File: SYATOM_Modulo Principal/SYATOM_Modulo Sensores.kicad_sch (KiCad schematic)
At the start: 27 parts, among them J1 Input, J10 Head_HX711_2, J11 Head_HX711, J12 Exp_GPIO, J13 Exp_ADC, J14 Exp_I2C, J15 PWM_A, J16 PWM_B, J17 Header_Max485_1, J18 Header_Max3232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

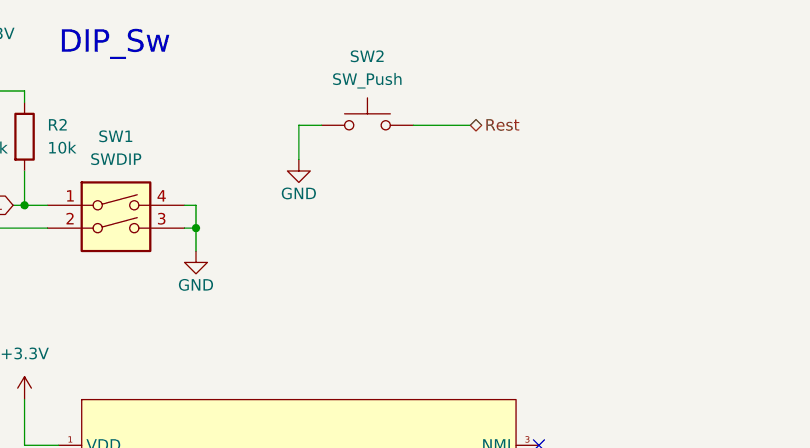
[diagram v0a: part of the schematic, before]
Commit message: Add files via upload
Se agrego el silkscreen de los logos y label de los conectores, ademas una resistencia pull-up al botón reset
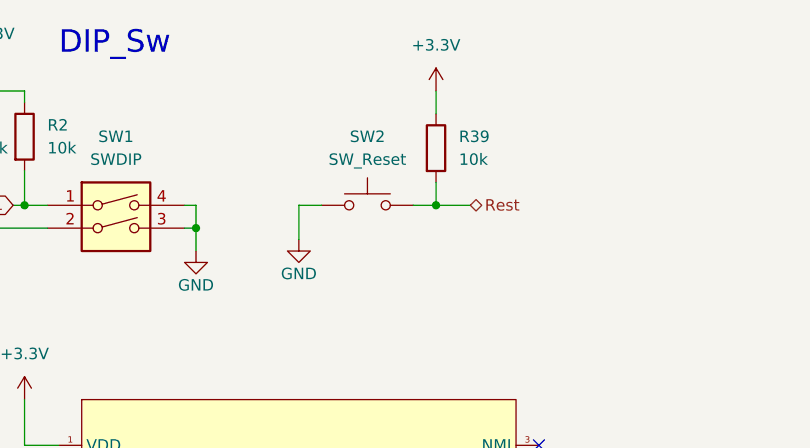
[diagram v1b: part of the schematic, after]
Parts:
- added R39: 10k, Resistor_SMD:R_0603_1608Metric, symbol Device:R
- SW2: value SW_Push -> SW_Reset
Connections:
- net +3V3: now also R39.1
- net Rest: now also R39.2
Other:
- moved on the sheet: SW2
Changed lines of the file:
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@@
   (junction (at 31.75 123.19) (diameter 0) (color 0 0 0 0)
+  )
+  (junction (at 194.31 38.1) (diameter 0) (color 0 0 0 0)
   )
   (junction (at 35.56 106.68) (diameter 0) (color 0 0 0 0)
@@
     (stroke (width 0) (type default) (color 0 0 0 0))
   )
-  (wire (pts (xy 179.07 29.21) (xy 179.07 33.02))
+  (wire (pts (xy 179.07 38.1) (xy 179.07 41.91))
     (stroke (width 0) (type default) (color 0 0 0 0))
   )
@@
     (stroke (width 0) (type default) (color 0 0 0 0))
   )
+  (wire (pts (xy 194.31 25.4) (xy 194.31 27.94))
+    (stroke (width 0) (type default) (color 0 0 0 0))
+  )
   (wire (pts (xy 205.74 104.14) (xy 214.63 104.14))
     (stroke (width 0) (type default) (color 0 0 0 0))
@@
     (stroke (width 0) (type default) (color 0 0 0 0))
   )
-  (wire (pts (xy 181.61 29.21) (xy 179.07 29.21))
+  (wire (pts (xy 181.61 38.1) (xy 179.07 38.1))
     (stroke (width 0) (type default) (color 0 0 0 0))
   )
@@
     (stroke (width 0) (type default) (color 0 0 0 0))
   )
+  (wire (pts (xy 194.31 38.1) (xy 198.12 38.1))
+    (stroke (width 0) (type default) (color 0 0 0 0))
+  )
   (wire (pts (xy 140.97 128.27) (xy 152.4 128.27))
     (stroke (width 0) (type default) (color 0 0 0 0))
@@
     (stroke (width 0) (type default) (color 0 0 0 0))
   )
+  (wire (pts (xy 194.31 35.56) (xy 194.31 38.1))
+    (stroke (width 0) (type default) (color 0 0 0 0))
+  )
   (wire (pts (xy 293.37 68.58) (xy 298.45 68.58))
     (stroke (width 0) (type default) (color 0 0 0 0))
@@
     (stroke (width 0) (type default) (color 0 0 0 0))
   )
-  (wire (pts (xy 191.77 29.21) (xy 198.12 29.21))
+  (wire (pts (xy 191.77 38.1) (xy 194.31 38.1))
     (stroke (width 0) (type default) (color 0 0 0 0))
   )
@@
     (effects (font (size 1.27 1.27)) (justify right))
   )
-  (hierarchical_label "Rest" (shape bidirectional) (at 198.12 29.21 0)
+  (hierarchical_label "Rest" (shape bidirectional) (at 198.12 38.1 0)
     (effects (font (size 1.27 1.27)) (justify left))
   )
@@
     (pin "3")
   )
+  (symbol (lib_id "Device:R") (at 194.31 31.75 0) (unit 1)
+    (in_bom yes) (on_board yes) (fields_autoplaced)
+    (property "Reference" "R39" (id 0) (at 196.85 30.4799 0)
+      (effects (font (size 1.27 1.27)) (justify left))
+    )
+    (property "Value" "10k" (id 1) (at 196.85 33.0199 0)
+      (effects (font (size 1.27 1.27)) (justify left))
+    )
+    (property "Footprint" "Resistor_SMD:R_0603_1608Metric" (id 2) (at 192.532 31.75 90)
+      (effects (font (size 1.27 1.27)) hide)
+    )
+    (property "Datasheet" "~" (id 3) (at 194.31 31.75 0)
+      (effects (font (size 1.27 1.27)) hide)
+    )
+    (pin "1")
+    (pin "2")
+  )
   (symbol (lib_id "Connector:Conn_01x04_Female") (at 76.2 176.53 270) (unit 1)
     (in_bom yes) (on_board yes)
@@
     (pin "4")
   )
-  (symbol (lib_id "power:GND") (at 179.07 33.02 0) (mirror y) (unit 1)
-    (in_bom yes) (on_board yes)
-    (property "Reference" "#PWR0106" (id 0) (at 179.07 39.37 0)
-      (effects (font (size 1.27 1.27)) hide)
-    )
-    (property "Value" "GND" (id 1) (at 179.07 36.83 0))
-    (property "Footprint" "" (id 2) (at 179.07 33.02 0)
-      (effects (font (size 1.27 1.27)) hide)
-    )
-    (property "Datasheet" "" (id 3) (at 179.07 33.02 0)
+  (symbol (lib_id "power:GND") (at 179.07 41.91 0) (mirror y) (unit 1)
+    (in_bom yes) (on_board yes)
+    (property "Reference" "#PWR0106" (id 0) (at 179.07 48.26 0)
+      (effects (font (size 1.27 1.27)) hide)
+    )
+    (property "Value" "GND" (id 1) (at 179.07 45.72 0))
+    (property "Footprint" "" (id 2) (at 179.07 41.91 0)
+      (effects (font (size 1.27 1.27)) hide)
+    )
+    (property "Datasheet" "" (id 3) (at 179.07 41.91 0)
       (effects (font (size 1.27 1.27)) hide)
     )
@@
     (pin "4")
   )
-  (symbol (lib_id "Switch:SW_Push") (at 186.69 29.21 0) (unit 1)
+  (symbol (lib_id "Switch:SW_Push") (at 186.69 38.1 0) (unit 1)
     (in_bom yes) (on_board yes) (fields_autoplaced)
-    (property "Reference" "SW2" (id 0) (at 186.69 21.59 0))
-    (property "Value" "SW_Push" (id 1) (at 186.69 24.13 0))
-    (property "Footprint" "Button_Switch_SMD:SW_SPST_B3S-1000" (id 2) (at 186.69 24.13 0)
-      (effects (font (size 1.27 1.27)) hide)
-    )
-    (property "Datasheet" "~" (id 3) (at 186.69 24.13 0)
+    (property "Reference" "SW2" (id 0) (at 186.69 30.48 0))
+    (property "Value" "SW_Reset" (id 1) (at 186.69 33.02 0))
+    (property "Footprint" "Button_Switch_SMD:SW_SPST_B3S-1000" (id 2) (at 186.69 33.02 0)
+      (effects (font (size 1.27 1.27)) hide)
+    )
+    (property "Datasheet" "~" (id 3) (at 186.69 33.02 0)
       (effects (font (size 1.27 1.27)) hide)
     )
@@
     (pin "5")
   )
+  (symbol (lib_id "power:+3.3V") (at 194.31 25.4 0) (unit 1)
+    (in_bom yes) (on_board yes) (fields_autoplaced)
+    (property "Reference" "#PWR0103" (id 0) (at 194.31 29.21 0)
+      (effects (font (size 1.27 1.27)) hide)
+    )
+    (property "Value" "+3.3V" (id 1) (at 194.31 20.32 0))
+    (property "Footprint" "" (id 2) (at 194.31 25.4 0)
+      (effects (font (size 1.27 1.27)) hide)
+    )
+    (property "Datasheet" "" (id 3) (at 194.31 25.4 0)
+      (effects (font (size 1.27 1.27)) hide)
+    )
+    (pin "1")
+  )
   (symbol (lib_id "Device:R") (at 140.97 30.48 0) (unit 1)
     (in_bom yes) (on_board yes) (fields_autoplaced)
@@
       (reference "#PWR0102") (unit 1) (value "GND") (footprint "")
     )
+    (path "/93cfea37-a71c-4dd7-b19e-d74de7abc00d"
+      (reference "#PWR0103") (unit 1) (value "+3.3V") (footprint "")
+    )
     (path "/c0d05a56-130f-4c1b-a894-60a4c461c4cf"
       (reference "#PWR0104") (unit 1) (value "+3.3V") (footprint "")
@@
       (reference "R38") (unit 1) (value "10") (footprint "Resistor_SMD:R_0603_1608Metric")
     )
+    (path "/2cc3fc2d-e26b-4791-a2da-ce038e944bb0"
+      (reference "R39") (unit 1) (value "10k") (footprint "Resistor_SMD:R_0603_1608Metric")
+    )
     (path "/3cab5223-6d87-437e-b44a-6453332dab28/567c9df1-7e2c-464f-9ad5-c1966717b3a6"
       (reference "R40") (unit 1) (value "10") (footprint "Resistor_SMD:R_0603_1608Metric")
@@
     )
     (path "/5e0e5e04-5dcf-46c7-8587-ae3bff279ac3"
-      (reference "SW2") (unit 1) (value "SW_Push") (footprint "Button_Switch_SMD:SW_SPST_B3S-1000")
+      (reference "SW2") (unit 1) (value "SW_Reset") (footprint "Button_Switch_SMD:SW_SPST_B3S-1000")
     )
     (path "/dd43f81b-2239-4953-b5a7-061614b97e20/d510debd-c265-4a0d-a801-9314fabe83b7"
